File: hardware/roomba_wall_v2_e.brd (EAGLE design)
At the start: 29.2 x 26.8 mm, 13 parts, among them T1 BC846, U1 ATTINY45V-10SU

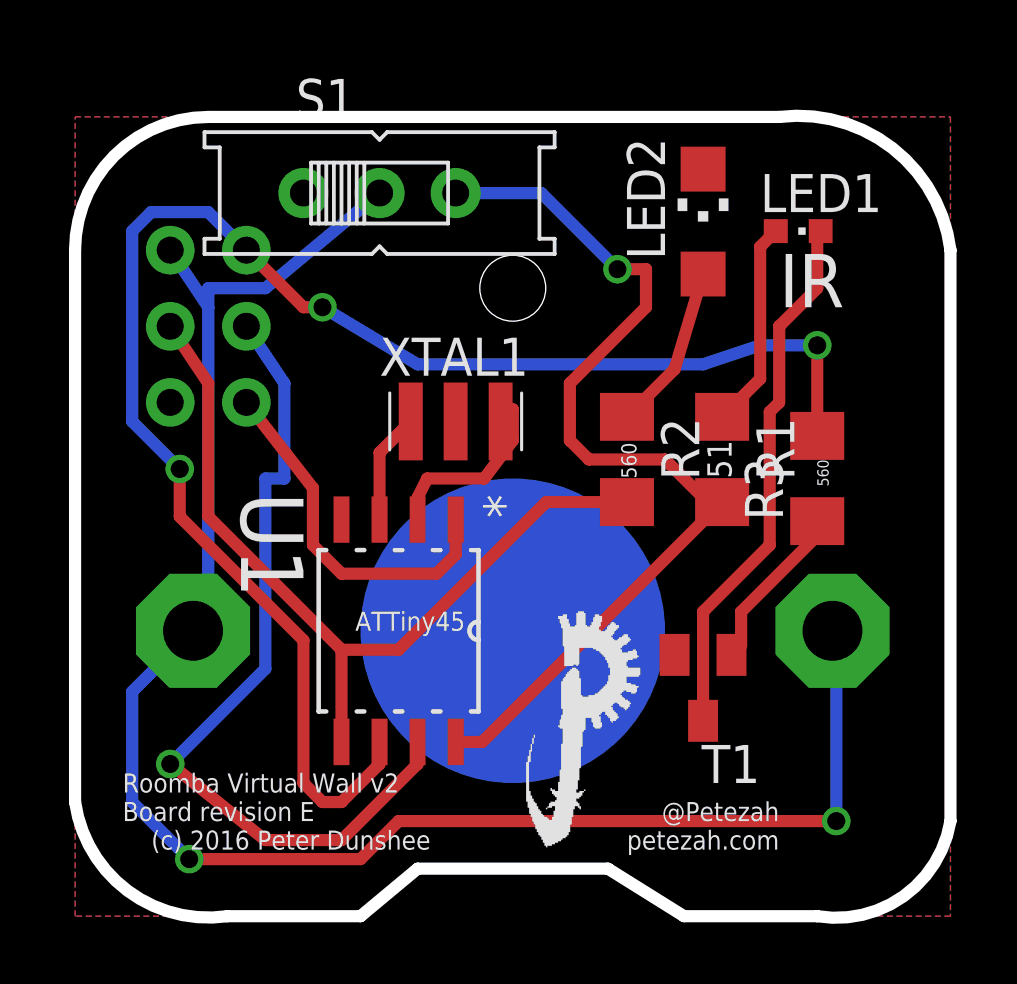
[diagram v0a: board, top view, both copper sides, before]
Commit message: Latest changes to rev E Not sure what's in here; they were made a while ago and just weren't committed.  This is possibly the fix to the unconnected GND on the MCU.
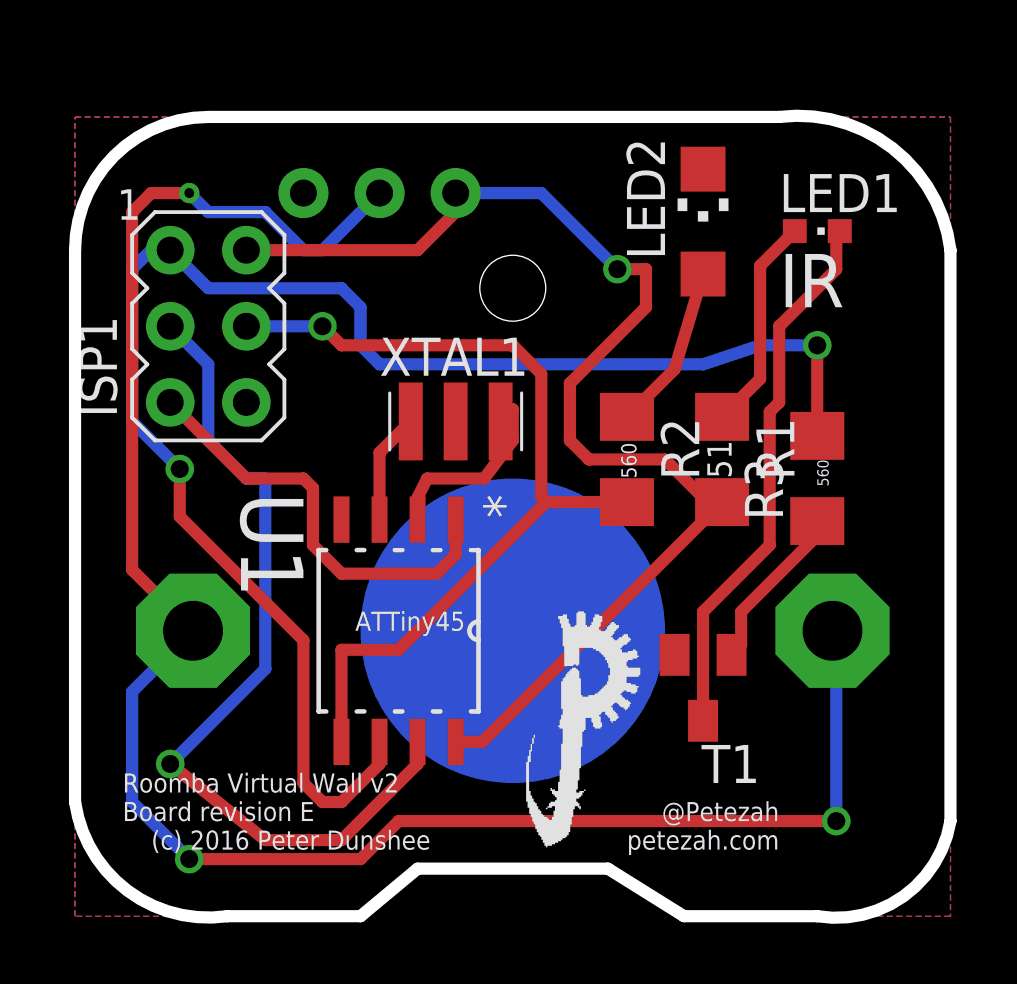
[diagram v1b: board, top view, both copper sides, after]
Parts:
- moved LED1 0.64 mm to (23.5, 22.9)
- flipped ISP1 to the top
- flipped S1 to the bottom
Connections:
- net +3V3: no longer ISP1.2
- net GND: now also U1.4
- net VCC: now also ISP1.2, S1.O; no longer S1.S
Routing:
- net VCC: track 32.4 -> 40.5 mm
- net +3V3: track 59.0 -> 62.8 mm, vias 2 -> 3
- net RST: track 12.1 -> 14.4 mm
- net MOSI: track 27.7 -> 29.5 mm, vias 0 -> 1
- net MISO: track 53.5 -> 52.7 mm, vias 3 -> 2
- net SCK: track 27.9 -> 28.5 mm
